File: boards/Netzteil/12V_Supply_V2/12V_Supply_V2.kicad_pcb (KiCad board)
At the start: 2 copper layers, 90 x 66 mm, 51 parts, among them P1 12V_AC, P2 12V_DC_1, P3 12V_DC_2, P4 Relais, P5 12V_DC_3, P6 12V_DC_4, P7 Relais, Q1 BS170, U1 LM393, U2 LM7812CT

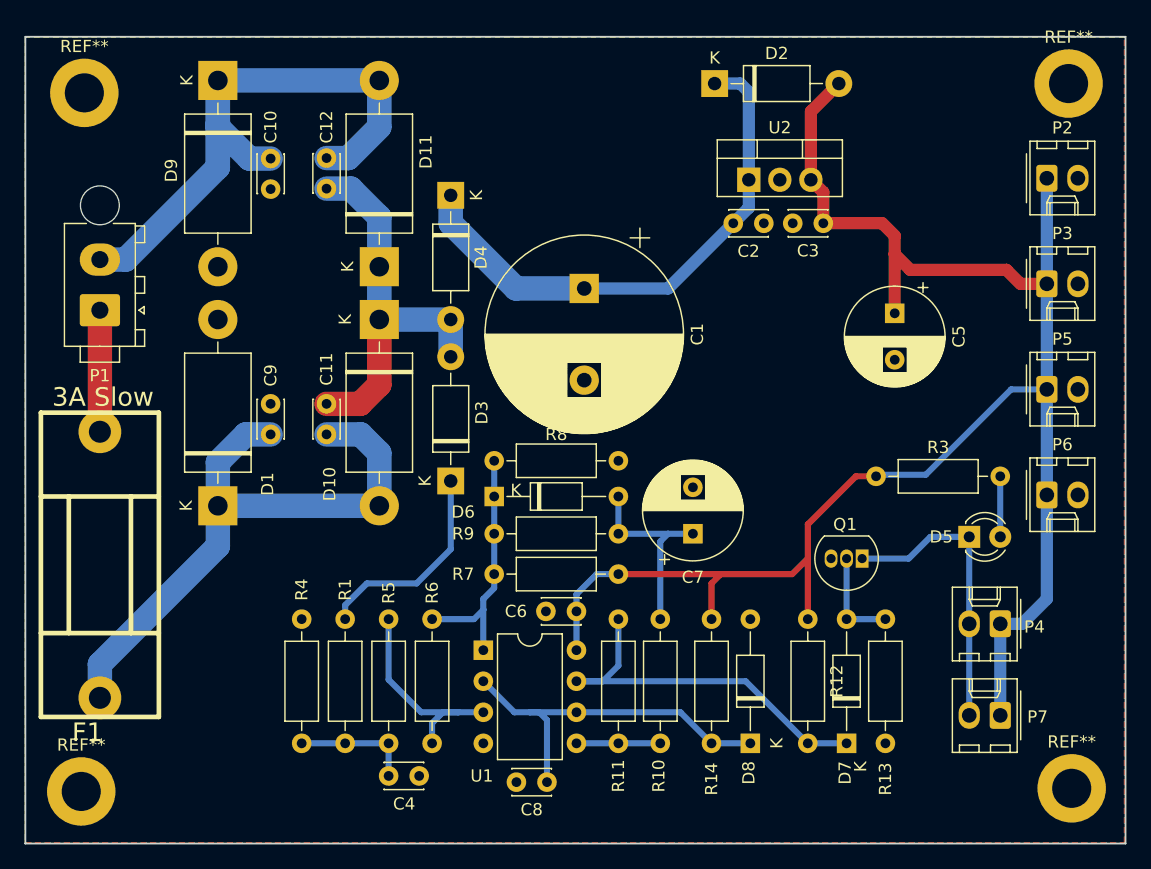
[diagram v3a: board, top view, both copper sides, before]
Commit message: Added Vias & Mounting Holes
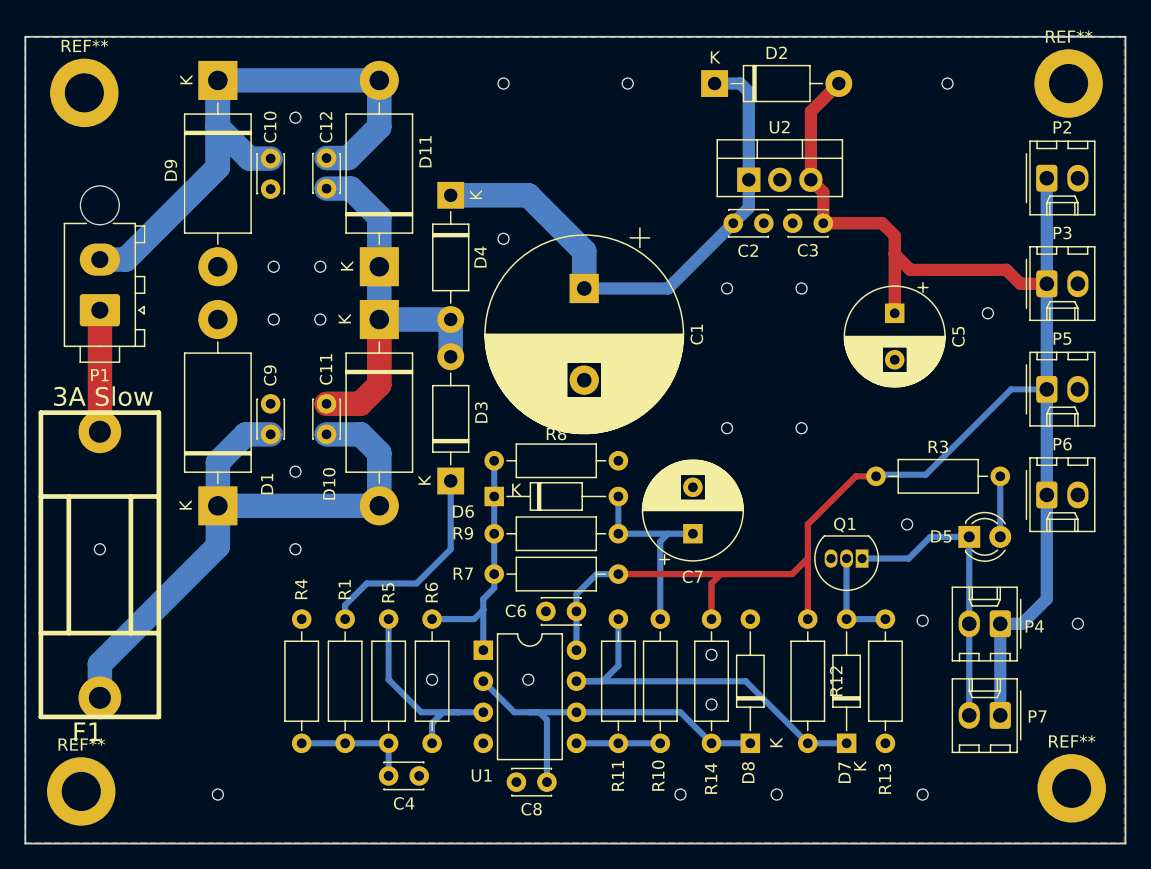
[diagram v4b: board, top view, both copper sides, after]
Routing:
- net GND: vias 0 -> 28
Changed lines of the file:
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@@
     (thickness 1.6)
     (drawings 4)
-    (tracks 131)
+    (tracks 159)
     (zones 0)
     (modules 51)
@@
   )
   (setup
-    (last_trace_width 2)
+    (last_trace_width 0.5)
     (user_trace_width 0.5)
     (user_trace_width 1)
@@
   (gr_line (start 180.17 113.228) (end 180.17 47.228) (layer Edge.Cuts) (width 0.15))
   (gr_line (start 90.17 113.228) (end 180.17 113.228) (layer Edge.Cuts) (width 0.15))
-  (segment (start 130.302 67.818) (end 135.89 67.818) (width 2) (layer B.Cu) (net 1))
-  (segment (start 124.968 60.198) (end 124.968 62.484) (width 2) (layer B.Cu) (net 1))
-  (segment (start 124.968 62.484) (end 130.302 67.818) (width 2) (layer B.Cu) (net 1))
   (segment (start 142.748 67.818) (end 148.082 62.484) (width 1) (layer B.Cu) (net 1))
   (segment (start 135.89 67.818) (end 142.748 67.818) (width 1) (layer B.Cu) (net 1))
@@
   (segment (start 149.352 51.748) (end 148.658 51.054) (width 1) (layer B.Cu) (net 1))
   (segment (start 149.352 58.928) (end 149.352 51.748) (width 1) (layer B.Cu) (net 1))
+  (segment (start 135.89 64.77) (end 135.89 67.818) (width 2) (layer B.Cu) (net 1))
+  (segment (start 124.968 60.198) (end 131.318 60.198) (width 2) (layer B.Cu) (net 1))
+  (segment (start 131.318 60.198) (end 135.89 64.77) (width 2) (layer B.Cu) (net 1))
+  (via (at 110.49 66.04) (size 1) (drill 0.8) (layers F.Cu B.Cu) (net 2))
+  (via (at 114.3 66.04) (size 1) (drill 0.8) (layers F.Cu B.Cu) (net 2))
+  (via (at 114.3 70.358) (size 1) (drill 0.8) (layers F.Cu B.Cu) (net 2))
+  (via (at 110.49 70.358) (size 1) (drill 0.8) (layers F.Cu B.Cu) (net 2))
+  (via (at 147.574 67.818) (size 1) (drill 0.8) (layers F.Cu B.Cu) (net 2))
+  (via (at 147.574 79.248) (size 1) (drill 0.8) (layers F.Cu B.Cu) (net 2))
+  (via (at 153.67 79.248) (size 1) (drill 0.8) (layers F.Cu B.Cu) (net 2))
+  (via (at 153.67 67.818) (size 1) (drill 0.8) (layers F.Cu B.Cu) (net 2))
+  (via (at 168.91 69.85) (size 1) (drill 0.8) (layers F.Cu B.Cu) (net 2))
+  (via (at 163.576 94.996) (size 1) (drill 0.8) (layers F.Cu B.Cu) (net 2))
+  (via (at 143.764 109.22) (size 1) (drill 0.8) (layers F.Cu B.Cu) (net 2))
+  (via (at 151.638 109.22) (size 1) (drill 0.8) (layers F.Cu B.Cu) (net 2))
+  (via (at 112.268 89.154) (size 1) (drill 0.8) (layers F.Cu B.Cu) (net 2))
+  (via (at 112.268 53.848) (size 1) (drill 0.8) (layers F.Cu B.Cu) (net 2))
+  (via (at 129.286 51.054) (size 1) (drill 0.8) (layers F.Cu B.Cu) (net 2))
+  (via (at 139.446 51.054) (size 1) (drill 0.8) (layers F.Cu B.Cu) (net 2))
+  (via (at 165.608 51.054) (size 1) (drill 0.8) (layers F.Cu B.Cu) (net 2))
+  (via (at 176.276 95.25) (size 1) (drill 0.8) (layers F.Cu B.Cu) (net 2))
+  (via (at 129.286 63.754) (size 1) (drill 0.8) (layers F.Cu B.Cu) (net 2))
+  (via (at 123.444 99.822) (size 1) (drill 0.8) (layers F.Cu B.Cu) (net 2))
+  (via (at 131.318 99.822) (size 1) (drill 0.8) (layers F.Cu B.Cu) (net 2))
+  (via (at 146.304 101.854) (size 1) (drill 0.8) (layers F.Cu B.Cu) (net 2))
+  (via (at 146.304 97.79) (size 1) (drill 0.8) (layers F.Cu B.Cu) (net 2))
+  (via (at 162.306 87.122) (size 1) (drill 0.8) (layers F.Cu B.Cu) (net 2))
+  (via (at 96.266 89.154) (size 1) (drill 0.8) (layers F.Cu B.Cu) (net 2))
+  (via (at 112.268 82.804) (size 1) (drill 0.8) (layers F.Cu B.Cu) (net 2))
+  (via (at 163.576 109.22) (size 1) (drill 0.8) (layers F.Cu B.Cu) (net 2))
+  (via (at 105.918 109.22) (size 1) (drill 0.8) (layers F.Cu B.Cu) (net 2))
   (segment (start 135.255 97.409) (end 135.255 94.234) (width 0.5) (layer B.Cu) (net 3) (status 30))
   (segment (start 169.926 95.25) (end 169.926 102.743) (width 1) (layer B.Cu) (net 3) (status 30))
@@
   (segment (start 161.29 69.85) (end 161.29 65.024) (width 1) (layer F.Cu) (net 3))
   (segment (start 161.29 65.024) (end 161.29 63.5) (width 1) (layer F.Cu) (net 3))
-  (segment (start 159.766 83.058) (end 159.766 83.185) (width 0.5) (layer B.Cu) (net 3))
-  (segment (start 163.83 83.058) (end 159.766 83.058) (width 0.5) (layer B.Cu) (net 3))
-  (segment (start 173.736 76.073) (end 170.815 76.073) (width 0.5) (layer B.Cu) (net 3))
-  (segment (start 170.815 76.073) (end 163.83 83.058) (width 0.5) (layer B.Cu) (net 3))
   (segment (start 162.56 66.294) (end 161.29 65.024) (width 1) (layer F.Cu) (net 3))
   (segment (start 170.434 66.294) (end 162.56 66.294) (width 1) (layer F.Cu) (net 3))
   (segment (start 173.736 67.437) (end 171.577 67.437) (width 1) (layer F.Cu) (net 3))
   (segment (start 171.577 67.437) (end 170.434 66.294) (width 1) (layer F.Cu) (net 3))
+  (segment (start 170.815 76.073) (end 163.83 83.058) (width 0.5) (layer B.Cu) (net 3))
+  (segment (start 173.736 76.073) (end 170.815 76.073) (width 0.5) (layer B.Cu) (net 3))
+  (segment (start 163.83 83.058) (end 159.766 83.058) (width 0.5) (layer B.Cu) (net 3))
+  (segment (start 159.766 83.058) (end 159.766 83.185) (width 0.5) (layer B.Cu) (net 3))
   (segment (start 112.776 105.029) (end 116.332 105.029) (width 0.5) (layer B.Cu) (net 4) (status 30))
   (segment (start 116.332 105.029) (end 119.888 105.029) (width 0.5) (layer B.Cu) (net 4) (status 30))

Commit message: Added Test, moved mounting holes
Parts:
- removed the REF** at (175.8, 108.7)
- removed the REF** at (94.7, 109.0)
- removed the REF** at (175.5, 51.1)
- removed the REF** at (95.0, 51.8)
- added G***: LOGO, Loewe:Loewe_Klein, F.Cu at (135.1, 55.1)
- added REF**: MountingHole_3.2mm_M3_DIN965, MountingHole:MountingHole_3.2mm_M3_DIN965, F.Cu at (95.2, 52.2)
- added REF**: MountingHole_3.2mm_M3_DIN965, MountingHole:MountingHole_3.2mm_M3_DIN965, F.Cu at (175.1, 52.2)
- added REF**: MountingHole_3.2mm_M3_DIN965, MountingHole:MountingHole_3.2mm_M3_DIN965, F.Cu at (175.1, 108.3)
- added REF**: MountingHole_3.2mm_M3_DIN965, MountingHole:MountingHole_3.2mm_M3_DIN965, F.Cu at (95.2, 108.3)
- moved C5 5.85 mm to (155.4, 69.6)
- moved Q1 3.18 mm to (161.8, 89.9)
- moved P3 2.59 mm to (174.2, 70.0)
- moved P5 2.59 mm to (174.2, 78.6)
- moved P2 2.59 mm to (174.2, 61.3)
- moved P6 2.59 mm to (174.2, 87.2)
- moved P7 2.29 mm to (169.9, 105.0)
- moved P4 1.52 mm to (169.9, 96.8)
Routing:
- net +12V: track 146.1 -> 147.7 mm
- net Net-(D5-Pad1): track 24.1 -> 23.2 mm
- net GND: vias 28 -> 29
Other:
- board text added: "12,5V AC In"
- board text added: "12V DC Out"
- board text added: "Amp. Enable"
